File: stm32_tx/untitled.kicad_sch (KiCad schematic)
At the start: 14 parts, among them U11 AMC1351DWV, U3 AMC1351DWV, U9 ACS709xLFTR-20BB

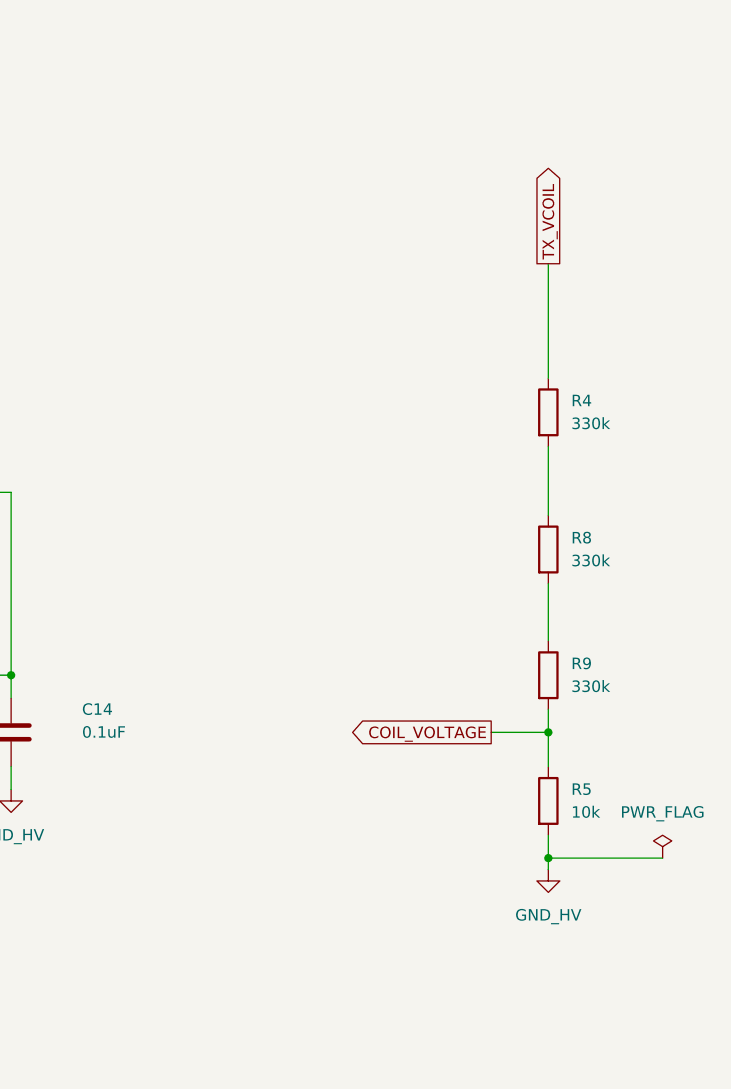
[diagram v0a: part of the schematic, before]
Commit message: Added components and structure for analogue overvoltage and overcurrent protection
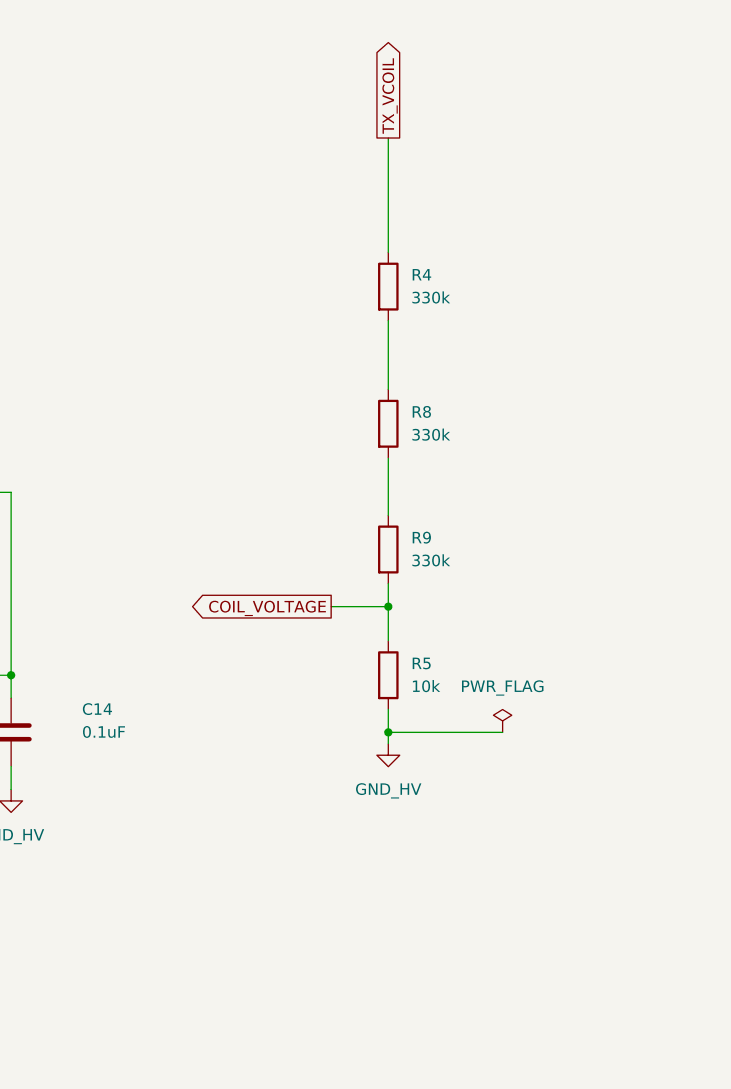
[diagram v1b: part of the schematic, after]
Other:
- moved on the sheet: R4, R5, R8, R9
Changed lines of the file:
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@@
 	)
 	(junction
-		(at 231.14 111.76)
+		(at 213.36 97.79)
 		(diameter 0)
 		(color 0 0 0 0)
 	)
 	(junction
-		(at 231.14 97.79)
+		(at 213.36 83.82)
 		(diameter 0)
 		(color 0 0 0 0)
@@
 	(wire
 		(pts
-			(xy 231.14 97.79) (xy 231.14 101.6)
+			(xy 213.36 83.82) (xy 213.36 87.63)
 		)
 		(stroke
@@
 	(wire
 		(pts
-			(xy 243.84 111.76) (xy 231.14 111.76)
-		)
-		(stroke
-			(width 0)
-			(type default)
-		)
-	)
-	(wire
-		(pts
-			(xy 231.14 111.76) (xy 231.14 113.03)
+			(xy 226.06 97.79) (xy 213.36 97.79)
+		)
+		(stroke
+			(width 0)
+			(type default)
+		)
+	)
+	(wire
+		(pts
+			(xy 213.36 97.79) (xy 213.36 99.06)
 		)
 		(stroke
@@
 	(wire
 		(pts
-			(xy 224.79 97.79) (xy 231.14 97.79)
+			(xy 207.01 83.82) (xy 213.36 83.82)
 		)
 		(stroke
@@
 	(wire
 		(pts
-			(xy 231.14 109.22) (xy 231.14 111.76)
+			(xy 213.36 95.25) (xy 213.36 97.79)
 		)
 		(stroke
@@
 	(wire
 		(pts
-			(xy 231.14 45.72) (xy 231.14 58.42)
+			(xy 213.36 31.75) (xy 213.36 44.45)
 		)
 		(stroke
@@
 	(wire
 		(pts
-			(xy 231.14 81.28) (xy 231.14 87.63)
-		)
-		(stroke
-			(width 0)
-			(type default)
-		)
-	)
-	(wire
-		(pts
-			(xy 231.14 95.25) (xy 231.14 97.79)
+			(xy 213.36 67.31) (xy 213.36 73.66)
+		)
+		(stroke
+			(width 0)
+			(type default)
+		)
+	)
+	(wire
+		(pts
+			(xy 213.36 81.28) (xy 213.36 83.82)
 		)
 		(stroke
@@
 	(wire
 		(pts
-			(xy 231.14 66.04) (xy 231.14 73.66)
+			(xy 213.36 52.07) (xy 213.36 59.69)
 		)
 		(stroke
@@
 	(global_label "TX_VCOIL"
 		(shape output)
-		(at 231.14 45.72 90)
+		(at 213.36 31.75 90)
 		(fields_autoplaced yes)
 		(effects
@@
 		)
 		(property "Intersheetrefs" "${INTERSHEET_REFS}"
-			(at 231.14 34.2681 90)
+			(at 213.36 20.2981 90)
 			(effects
 				(font
@@
 	(global_label "COIL_VOLTAGE"
 		(shape output)
-		(at 224.79 97.79 180)
+		(at 207.01 83.82 180)
 		(fields_autoplaced yes)
 		(effects
@@
 		)
 		(property "Intersheetrefs" "${INTERSHEET_REFS}"
-			(at 208.6814 97.79 0)
+			(at 190.9014 83.82 0)
 			(effects
 				(font
@@
 	(symbol
 		(lib_id "power:GND")
-		(at 231.14 113.03 0)
+		(at 213.36 99.06 0)
 		(unit 1)
 		(exclude_from_sim no)
@@
 		(fields_autoplaced yes)
 		(property "Reference" "#PWR05"
-			(at 231.14 119.38 0)
+			(at 213.36 105.41 0)
 			(effects
 				(font
@@
 		)
 		(property "Value" "GND_HV"
-			(at 231.14 118.11 0)
+			(at 213.36 104.14 0)
 			(effects
 				(font
@@
 		)
 		(property "Footprint" ""
-			(at 231.14 113.03 0)
+			(at 213.36 99.06 0)
 			(effects
 				(font
@@
 		)
 		(property "Datasheet" ""
-			(at 231.14 113.03 0)
+			(at 213.36 99.06 0)
 			(effects
 				(font
@@
 		)
 		(property "Description" "Power symbol creates a global label with name \"GND\" , ground"
-			(at 231.14 113.03 0)
+			(at 213.36 99.06 0)
 			(effects
 				(font
@@
 	(symbol
 		(lib_id "Device:R")
-		(at 231.14 77.47 0)
+		(at 213.36 63.5 0)
 		(unit 1)
 		(exclude_from_sim no)
@@
 		(fields_autoplaced yes)
 		(property "Reference" "R8"
-			(at 233.68 76.1999 0)
+			(at 215.9 62.2299 0)
 			(effects
 				(font
@@
 		)
 		(property "Value" "330k"
-			(at 233.68 78.7399 0)
+			(at 215.9 64.7699 0)
 			(effects
 				(font
@@
 		)
 		(property "Footprint" ""
-			(at 229.362 77.47 90)
+			(at 211.582 63.5 90)
 			(effects
 				(font
@@
 		)
 		(property "Datasheet" "~"
-			(at 231.14 77.47 0)
+			(at 213.36 63.5 0)
 			(effects
 				(font
@@
 		)
 		(property "Description" "Resistor"
-			(at 231.14 77.47 0)
+			(at 213.36 63.5 0)
 			(effects
 				(font
@@
 	(symbol
 		(lib_id "Device:R")
-		(at 231.14 91.44 0)
+		(at 213.36 77.47 0)
 		(unit 1)
 		(exclude_from_sim no)
@@
 		(fields_autoplaced yes)
 		(property "Reference" "R9"
-			(at 233.68 90.1699 0)
+			(at 215.9 76.1999 0)
 			(effects
 				(font
@@
 		)
 		(property "Value" "330k"
-			(at 233.68 92.7099 0)
+			(at 215.9 78.7399 0)
 			(effects
 				(font
@@
 		)
 		(property "Footprint" ""
-			(at 229.362 91.44 90)
+			(at 211.582 77.47 90)
 			(effects
 				(font
@@
 		)
 		(property "Datasheet" "~"
-			(at 231.14 91.44 0)
+			(at 213.36 77.47 0)
 			(effects
 				(font
@@
 		)
 		(property "Description" "Resistor"
-			(at 231.14 91.44 0)
+			(at 213.36 77.47 0)
 			(effects
 				(font
@@
 	(symbol
 		(lib_id "Device:R")
-		(at 231.14 105.41 0)
+		(at 213.36 91.44 0)
 		(unit 1)
 		(exclude_from_sim no)
@@
 		(fields_autoplaced yes)
 		(property "Reference" "R5"
-			(at 233.68 104.1399 0)
+			(at 215.9 90.1699 0)
 			(effects
 				(font
@@
 		)
 		(property "Value" "10k"
-			(at 233.68 106.6799 0)
+			(at 215.9 92.7099 0)
 			(effects
 				(font
@@
 		)
 		(property "Footprint" ""
-			(at 229.362 105.41 90)
+			(at 211.582 91.44 90)
 			(effects
 				(font
@@
 		)
 		(property "Datasheet" "~"
-			(at 231.14 105.41 0)
+			(at 213.36 91.44 0)
 			(effects
 				(font
@@
 		)
 		(property "Description" "Resistor"
-			(at 231.14 105.41 0)
+			(at 213.36 91.44 0)
 			(effects
 				(font
@@
 	(symbol
 		(lib_id "power:PWR_FLAG")
-		(at 243.84 111.76 0)
+		(at 226.06 97.79 0)
 		(unit 1)
 		(exclude_from_sim no)
@@
 		(fields_autoplaced yes)
 		(property "Reference" "#FLG06"
-			(at 243.84 109.855 0)
+			(at 226.06 95.885 0)
 			(effects
 				(font
@@
 		)
 		(property "Value" "PWR_FLAG"
-			(at 243.84 106.68 0)
+			(at 226.06 92.71 0)
 			(effects
 				(font
@@
 		)
 		(property "Footprint" ""
-			(at 243.84 111.76 0)
+			(at 226.06 97.79 0)
 			(effects
 				(font
@@
 		)
 		(property "Datasheet" "~"
-			(at 243.84 111.76 0)
+			(at 226.06 97.79 0)
 			(effects
 				(font
@@
 		)
 		(property "Description" "Special symbol for telling ERC where power comes from"
-			(at 243.84 111.76 0)
+			(at 226.06 97.79 0)
 			(effects
 				(font
@@
 	(symbol
 		(lib_id "Device:R")
-		(at 231.14 62.23 0)
+		(at 213.36 48.26 0)
 		(unit 1)
 		(exclude_from_sim no)
@@
 		(fields_autoplaced yes)
 		(property "Reference" "R4"
-			(at 233.68 60.9599 0)
+			(at 215.9 46.9899 0)
 			(effects
 				(font
@@
 		)
 		(property "Value" "330k"
-			(at 233.68 63.4999 0)
+			(at 215.9 49.5299 0)
 			(effects
 				(font
@@
 		)
 		(property "Footprint" ""
-			(at 229.362 62.23 90)
+			(at 211.582 48.26 90)
 			(effects
 				(font
@@
 		)
 		(property "Datasheet" "~"
-			(at 231.14 62.23 0)
+			(at 213.36 48.26 0)
 			(effects
 				(font
@@
 		)
 		(property "Description" "Resistor"
-			(at 231.14 62.23 0)
-			(effects
-				(font
+			(at 213.36 48.26 0)
+			(effects
+				(font

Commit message: Added selected footprints
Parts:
- C13, C14, C15, C16: footprint (none) -> Capacitor_SMD:C_0402_1005Metric
- R4, R5, R8, R9: footprint (none) -> Resistor_SMD:R_1206_3216Metric
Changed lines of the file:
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@@
 			)
 		)
-		(property "Footprint" ""
+		(property "Footprint" "Resistor_SMD:R_1206_3216Metric"
 			(at 211.582 63.5 90)
 			(effects
@@
 			)
 		)
-		(property "Footprint" ""
+		(property "Footprint" "Capacitor_SMD:C_0402_1005Metric"
 			(at 146.3548 105.41 0)
 			(effects
@@
 			)
 		)
-		(property "Footprint" ""
+		(property "Footprint" "Capacitor_SMD:C_0402_1005Metric"
 			(at 155.2448 93.98 0)
 			(effects
@@
 			)
 		)
-		(property "Footprint" ""
+		(property "Footprint" "Resistor_SMD:R_1206_3216Metric"
 			(at 211.582 77.47 90)
 			(effects
@@
 			)
 		)
-		(property "Footprint" ""
+		(property "Footprint" "Resistor_SMD:R_1206_3216Metric"
 			(at 211.582 91.44 90)
 			(effects
@@
 			)
 		)
-		(property "Footprint" ""
+		(property "Footprint" "Capacitor_SMD:C_0402_1005Metric"
 			(at 170.4848 93.98 0)
 			(effects
@@
 			)
 		)
-		(property "Footprint" ""
+		(property "Footprint" "Resistor_SMD:R_1206_3216Metric"
 			(at 211.582 48.26 90)
 			(effects
@@
 			)
 		)
-		(property "Footprint" ""
+		(property "Footprint" "Capacitor_SMD:C_0402_1005Metric"
 			(at 151.4348 110.49 0)
 			(effects
